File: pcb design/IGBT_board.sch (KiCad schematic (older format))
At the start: 44 parts, among them Q1 IGBT, Q10 IGBT, Q11 IGBT, Q12 IGBT, Q2 IGBT, Q3 IGBT, Q4 IGBT, Q5 IGBT, Q6 IGBT, Q7 IGBT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

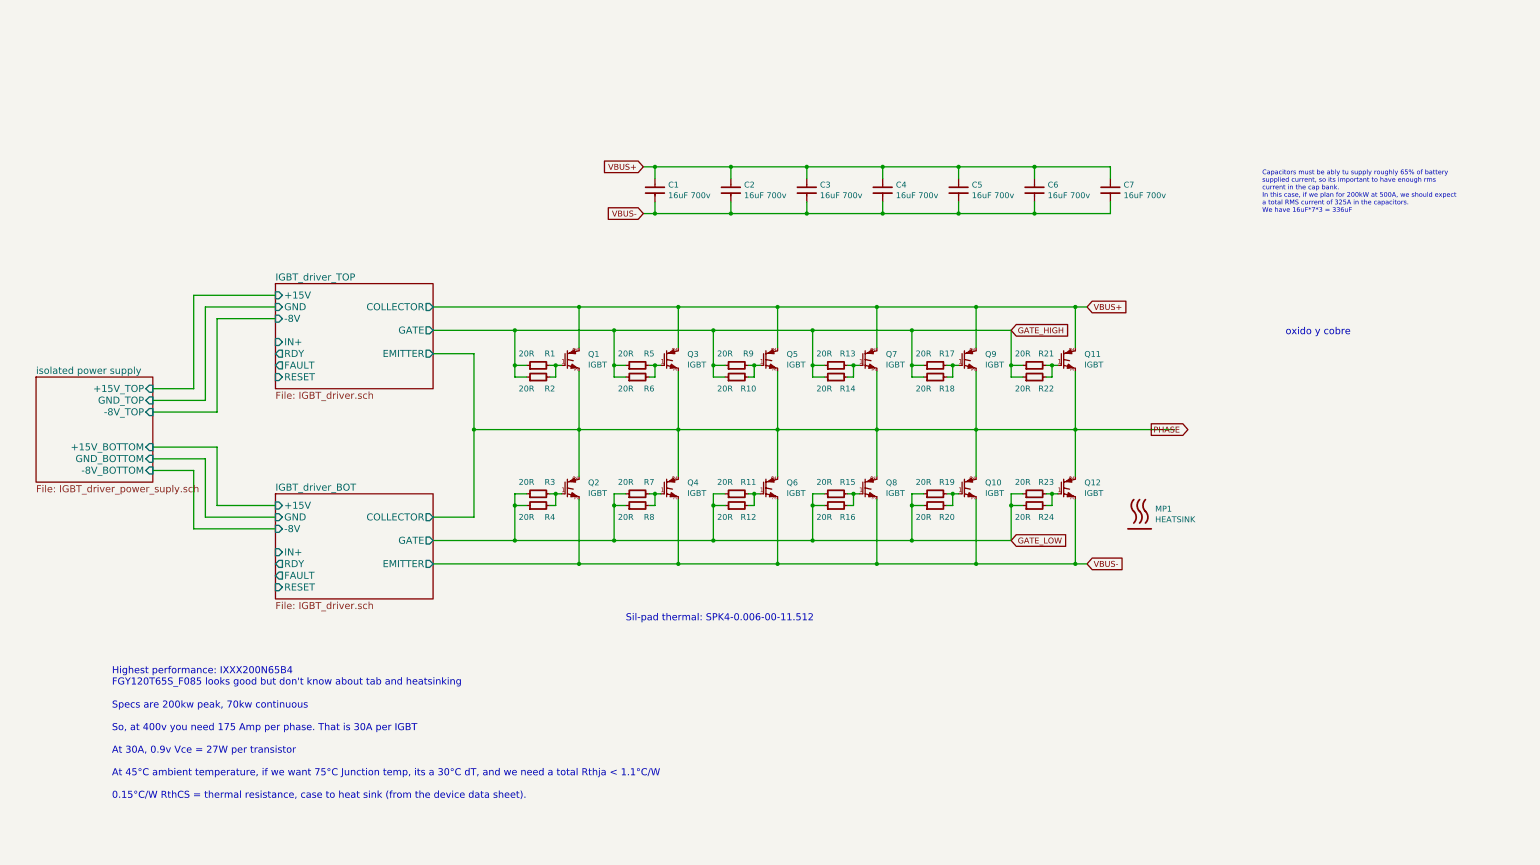
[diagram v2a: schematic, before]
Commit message: Add footprints, more layout and graphics
Signed-off-by: Marcos Chaparro <mchaparro@paltatech.com>
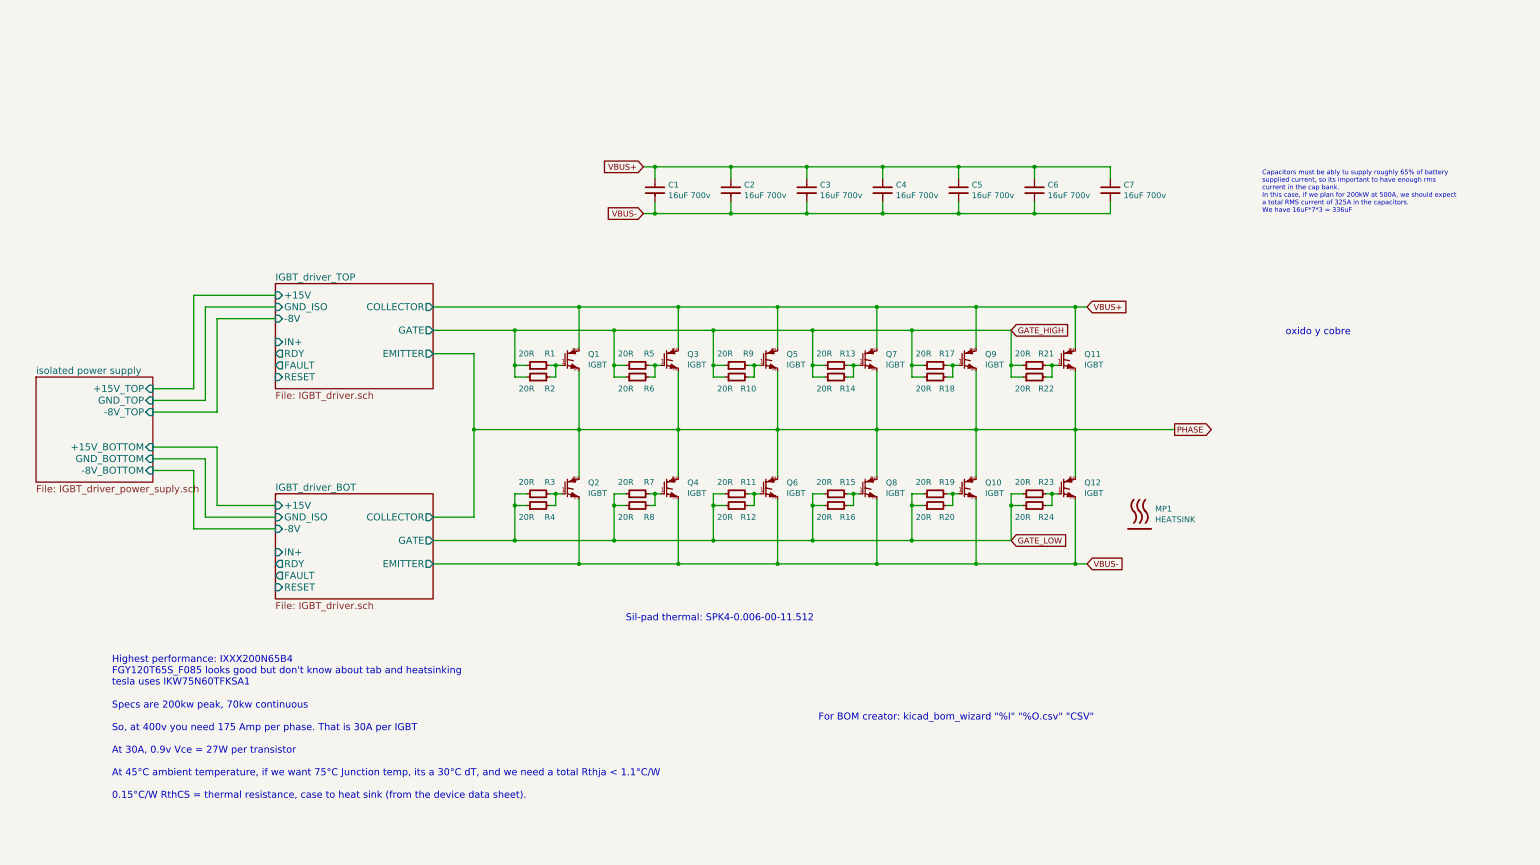
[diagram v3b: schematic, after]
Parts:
- Q10, Q11, Q12, Q2, Q3, Q4, Q5, Q6, Q7, Q8, Q9: mfg# IXXH80N65B4-ND -> IXXX110N65B4H1
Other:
- note added: "For BOM creator: kicad_bom_wizard "%I" "%O.csv" "CSV""
- note added: "Highest performance: IXXX200N65B4\nFGY120T65S_F085 looks good but don't know about tab and heatsinking\ntesla uses IKW75N60TFKSA1"
- note removed: "Highest performance: IXXX200N65B4\nFGY120T65S_F085 looks good but don't know about tab and heatsinking"
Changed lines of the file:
@@
 encoding utf-8
 Sheet 1 4
-Title ""
-Date ""
-Rev ""
-Comp ""
+Title "IGBT module"
+Date "2016-11-09"
+Rev "A"
+Comp "PALTA TECH"
 Comment1 ""
 Comment2 ""
@@
 F 2 "pth-semi:TO-247" H 6227 3409 60  0001 L CNN
 F 3 "" H 6100 3550 60  0000 C CNN
-F 4 "IXXH80N65B4-ND" H 6100 3500 60  0001 C CNN "mfg#"
+F 4 "IXXX110N65B4H1" H 6100 3500 60  0001 C CNN "mfg#"
 	1    6100 3500
 	1    0    0    -1
 $EndComp
 Text Notes 1300 6300 0    60   ~ 0
-Highest performance: IXXX200N65B4\nFGY120T65S_F085 looks good but don't know about tab and heatsinking
+Highest performance: IXXX200N65B4\nFGY120T65S_F085 looks good but don't know about tab and heatsinking\ntesla uses IKW75N60TFKSA1
 $Comp
 L R-2512 R1
@@
 F 2 "pth-semi:TO-247" H 5250 4650 60  0001 C CNN
 F 3 "" H 5250 4650 60  0000 C CNN
-F 4 "IXXH80N65B4-ND" H 5250 4600 60  0001 C CNN "mfg#"
+F 4 "IXXX110N65B4H1" H 5250 4600 60  0001 C CNN "mfg#"
 	1    5250 4600
 	1    0    0    -1
@@
 F 2 "pth-semi:TO-247" H 6100 4650 60  0001 C CNN
 F 3 "" H 6100 4650 60  0000 C CNN
-F 4 "IXXH80N65B4-ND" H 6100 4600 60  0001 C CNN "mfg#"
+F 4 "IXXX110N65B4H1" H 6100 4600 60  0001 C CNN "mfg#"
 	1    6100 4600
 	1    0    0    -1
@@
 F 2 "pth-semi:TO-247" H 7077 3409 60  0001 L CNN
 F 3 "" H 6950 3550 60  0000 C CNN
-F 4 "IXXH80N65B4-ND" H 6950 3500 60  0001 C CNN "mfg#"
+F 4 "IXXX110N65B4H1" H 6950 3500 60  0001 C CNN "mfg#"
 	1    6950 3500
 	1    0    0    -1
@@
 F 2 "pth-semi:TO-247" H 7800 3550 60  0001 C CNN
 F 3 "" H 7800 3550 60  0000 C CNN
-F 4 "IXXH80N65B4-ND" H 7800 3500 60  0001 C CNN "mfg#"
+F 4 "IXXX110N65B4H1" H 7800 3500 60  0001 C CNN "mfg#"
 	1    7800 3500
 	1    0    0    -1
@@
 F 2 "pth-semi:TO-247" H 6950 4650 60  0001 C CNN
 F 3 "" H 6950 4650 60  0000 C CNN
-F 4 "IXXH80N65B4-ND" H 6950 4600 60  0001 C CNN "mfg#"
+F 4 "IXXX110N65B4H1" H 6950 4600 60  0001 C CNN "mfg#"
 	1    6950 4600
 	1    0    0    -1
@@
 F 2 "pth-semi:TO-247" H 7800 4650 60  0001 C CNN
 F 3 "" H 7800 4650 60  0000 C CNN
-F 4 "IXXH80N65B4-ND" H 7800 4600 60  0001 C CNN "mfg#"
+F 4 "IXXX110N65B4H1" H 7800 4600 60  0001 C CNN "mfg#"
 	1    7800 4600
 	1    0    0    -1
@@
 F 2 "pth-semi:TO-247" H 8650 3550 60  0001 C CNN
 F 3 "" H 8650 3550 60  0000 C CNN
-F 4 "IXXH80N65B4-ND" H 8650 3500 60  0001 C CNN "mfg#"
+F 4 "IXXX110N65B4H1" H 8650 3500 60  0001 C CNN "mfg#"
 	1    8650 3500
 	1    0    0    -1
@@
 F 2 "pth-semi:TO-247" H 9500 3550 60  0001 C CNN
 F 3 "" H 9500 3550 60  0000 C CNN
-F 4 "IXXH80N65B4-ND" H 9500 3500 60  0001 C CNN "mfg#"
+F 4 "IXXX110N65B4H1" H 9500 3500 60  0001 C CNN "mfg#"
 	1    9500 3500
 	1    0    0    -1
@@
 F 2 "pth-semi:TO-247" H 8650 4650 60  0001 C CNN
 F 3 "" H 8650 4650 60  0000 C CNN
-F 4 "IXXH80N65B4-ND" H 8650 4600 60  0001 C CNN "mfg#"
+F 4 "IXXX110N65B4H1" H 8650 4600 60  0001 C CNN "mfg#"
 	1    8650 4600
 	1    0    0    -1
@@
 F 2 "pth-semi:TO-247" H 9500 4650 60  0001 C CNN
 F 3 "" H 9500 4650 60  0000 C CNN
-F 4 "IXXH80N65B4-ND" H 9500 4600 60  0001 C CNN "mfg#"
+F 4 "IXXX110N65B4H1" H 9500 4600 60  0001 C CNN "mfg#"
 	1    9500 4600
 	1    0    0    -1
@@
 GATE_LOW
 Connection ~ 4750 5050
-Text GLabel 10200 4100 2    50   Output ~ 0
+Text GLabel 10400 4100 2    50   Output ~ 0
 PHASE
 $Comp
@@
 F0 "IGBT_driver_TOP" 60
 F1 "IGBT_driver.sch" 60
-F2 "GND" I L 2700 3050 60
-F3 "+15V" I L 2700 2950 60
-F4 "-8V" I L 2700 3150 60
-F5 "IN+" I L 2700 3350 60
-F6 "GATE" O R 4050 3250 60
-F7 "COLLECTOR" O R 4050 3050 60
-F8 "EMITTER" O R 4050 3450 60
-F9 "RDY" O L 2700 3450 60
-F10 "FAULT" O L 2700 3550 60
-F11 "RESET" I L 2700 3650 60
+F2 "+15V" I L 2700 2950 60
+F3 "-8V" I L 2700 3150 60
+F4 "IN+" I L 2700 3350 60
+F5 "GATE" O R 4050 3250 60
+F6 "COLLECTOR" O R 4050 3050 60
+F7 "EMITTER" O R 4050 3450 60
+F8 "RDY" O L 2700 3450 60
+F9 "FAULT" O L 2700 3550 60
+F10 "RESET" I L 2700 3650 60
+F11 "GND_ISO" I L 2700 3050 60
 $EndSheet
 $Sheet
@@
 F0 "IGBT_driver_BOT" 60
 F1 "IGBT_driver.sch" 60
-F2 "GND" I L 2700 4850 60
-F3 "+15V" I L 2700 4750 60
-F4 "-8V" I L 2700 4950 60
-F5 "IN+" I L 2700 5150 60
-F6 "GATE" O R 4050 5050 60
-F7 "COLLECTOR" O R 4050 4850 60
-F8 "EMITTER" O R 4050 5250 60
-F9 "RDY" O L 2700 5250 60
-F10 "FAULT" O L 2700 5350 60
-F11 "RESET" I L 2700 5450 60
+F2 "+15V" I L 2700 4750 60
+F3 "-8V" I L 2700 4950 60
+F4 "IN+" I L 2700 5150 60
+F5 "GATE" O R 4050 5050 60
+F6 "COLLECTOR" O R 4050 4850 60
+F7 "EMITTER" O R 4050 5250 60
+F8 "RDY" O L 2700 5250 60
+F9 "FAULT" O L 2700 5350 60
+F10 "RESET" I L 2700 5450 60
+F11 "GND_ISO" I L 2700 4850 60
 $EndSheet
 Wire Wire Line
@@
 Wire Wire Line
 	2000 4450 1650 4450
+Text Notes 7350 6600 0    60   ~ 0
+For BOM creator: kicad_bom_wizard "%I" "%O.csv" "CSV"
 $EndSCHEMATC

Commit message: Larger gate resistors, added gate caps, added comments and images to the schematic
Signed-off-by: Marcos Chaparro <mchaparro@paltatech.com>
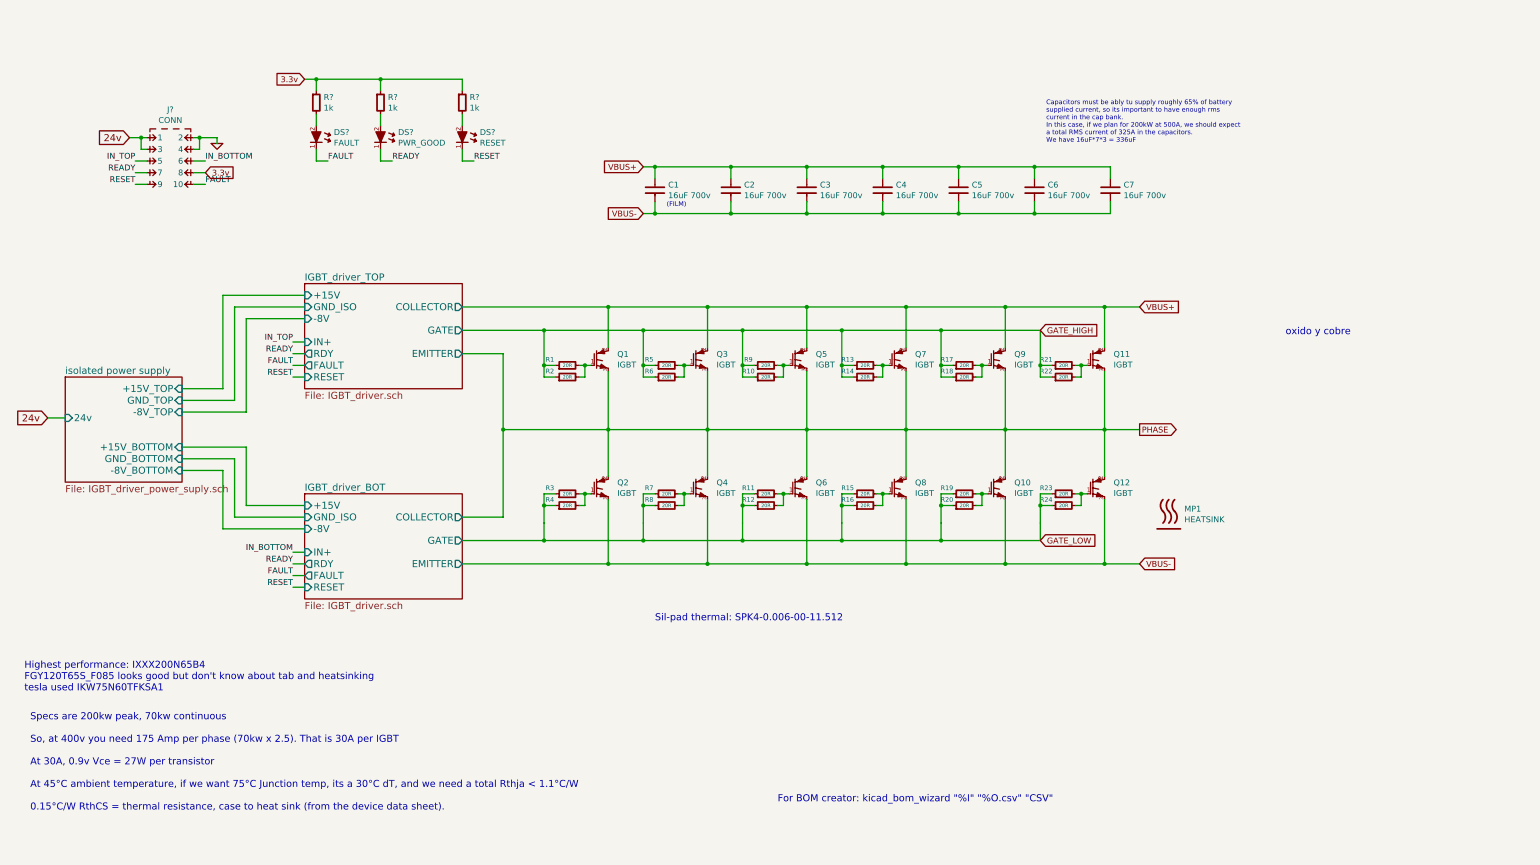
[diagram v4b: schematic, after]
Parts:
- added DS?: FAULT, smd-semi:LED-0603, symbol LED-0603
- added DS?: PWR_GOOD, smd-semi:LED-0603, symbol LED-0603
- added DS?: RESET, smd-semi:LED-0603, symbol LED-0603
- added J?: CONN, conn-100mil:CONN-100MIL-M-2x5, symbol CONN-100MIL-M-2x5
- added R? (x3): 1k, IPC7351-Nominal:RESC1608X50, symbol R-0603
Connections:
- new net: DS?.2 (A), R?.2 (x3)
- new net 24v: J?.1, J?.3
- new net 3.3v: J?.8, R?.1, R?.1, R?.1
- new net FAULT: DS?.1 (K), J?.10
- new net GND: J?.2, J?.4
- new net IN_BOTTOM: J?.6
- new net IN_TOP: J?.5
- new net READY: DS?.1 (K), J?.7
- new net RESET: DS?.1 (K), J?.9
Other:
- note added: "(FILM)"
- note added: "Highest performance: IXXX200N65B4\nFGY120T65S_F085 looks good but don't know about tab and heatsinking\ntesla used IKW75N60TFKSA1"
- note added: "Specs are 200kw peak, 70kw continuous\n\nSo, at 400v you need 175 Amp per phase (70kw x 2.5). That is 30A per IGBT\n\nAt 30A, 0.9v Vce = 27W per transistor\n\nAt 45°C ambient temperature, if we want 75°C Junction temp, its a 30°C dT, and we need a total Rthja < 1.1°C/W\n\n0.15°C/W RthCS = thermal resistance, case to heat sink (from the device data sheet). \n\n\n\n\n\n\n"
- note removed: "Highest performance: IXXX200N65B4\nFGY120T65S_F085 looks good but don't know about tab and heatsinking\ntesla uses IKW75N60TFKSA1"
- note removed: "Specs are 200kw peak, 70kw continuous\n\nSo, at 400v you need 175 Amp per phase. That is 30A per IGBT\n\nAt 30A, 0.9v Vce = 27W per transistor\n\nAt 45°C ambient temperature, if we want 75°C Junction temp, its a 30°C dT, and we need a total Rthja < 1.1°C/W\n\n0.15°C/W RthCS = thermal resistance, case to heat sink (from the device data sheet). \n\n\n\n\n\n\n"
- moved on the sheet: MP1, Q1, Q10, Q11, Q12, Q2, Q3, Q4, Q5, Q6, Q7, Q8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

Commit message: Added 3D models, connector, more layout, updated readme
Signed-off-by: Marcos Chaparro <mchaparro@paltatech.com>
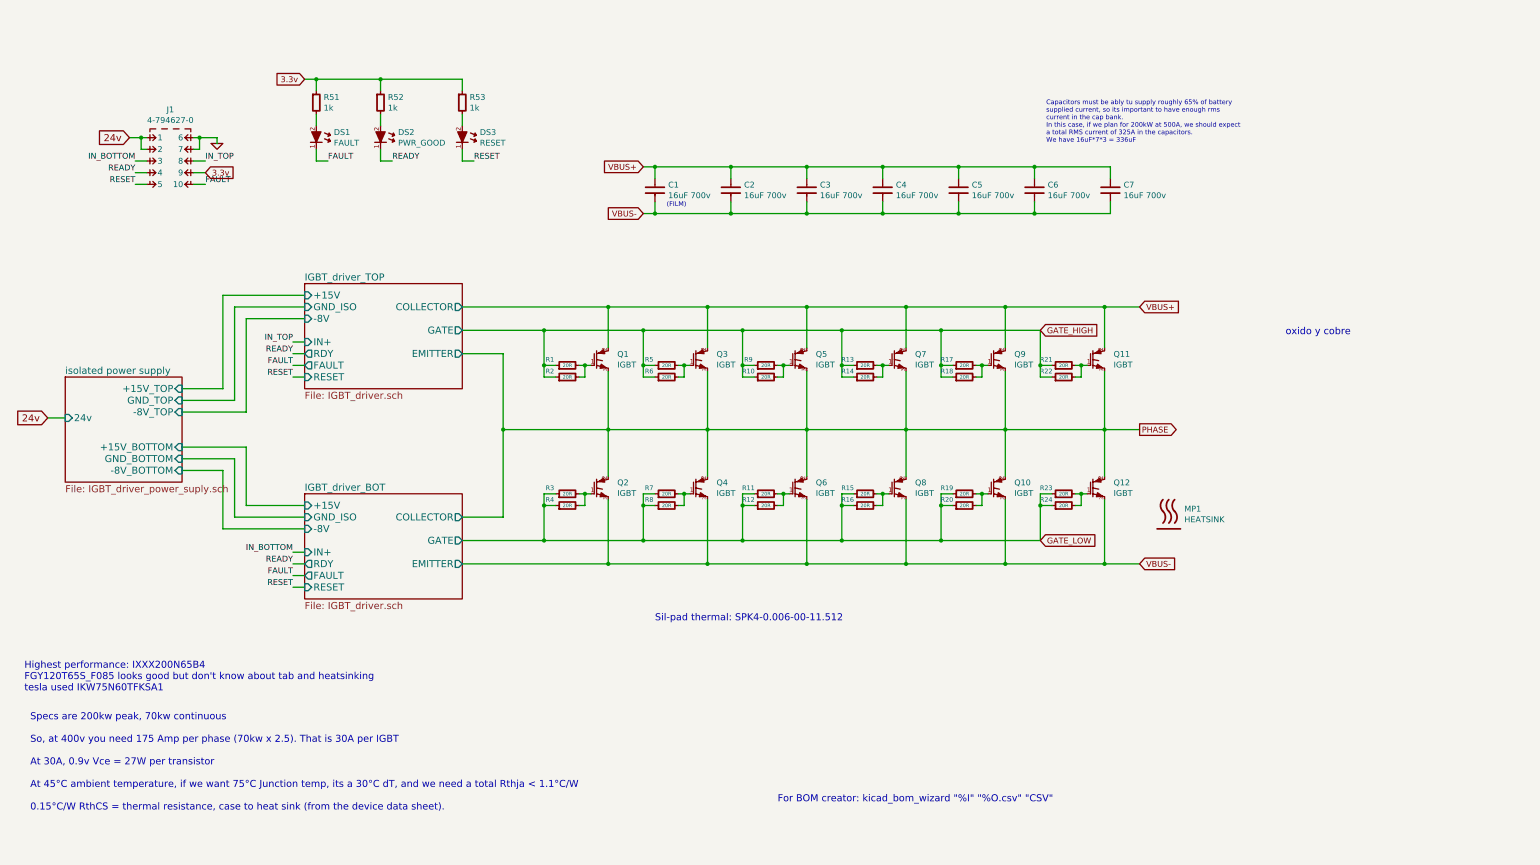
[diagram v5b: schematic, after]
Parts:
- removed J?: CONN, conn-100mil:CONN-100MIL-M-2x5, symbol CONN-100MIL-M-2x5
- added J1: 4-794627-0, paltatech:TE-4-794627-0, symbol 4-794627-0
- gave numbers to parts that had none: 6
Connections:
- net 24v: now also J1.1, J1.2
- net 3.3v: now also J1.9
- net FAULT: now also J1.10
- net GND: now also J1.6, J1.7
- net IN_BOTTOM: now also J1.3
- net IN_TOP: now also J1.8
- net READY: now also J1.4
- net RESET: now also J1.5

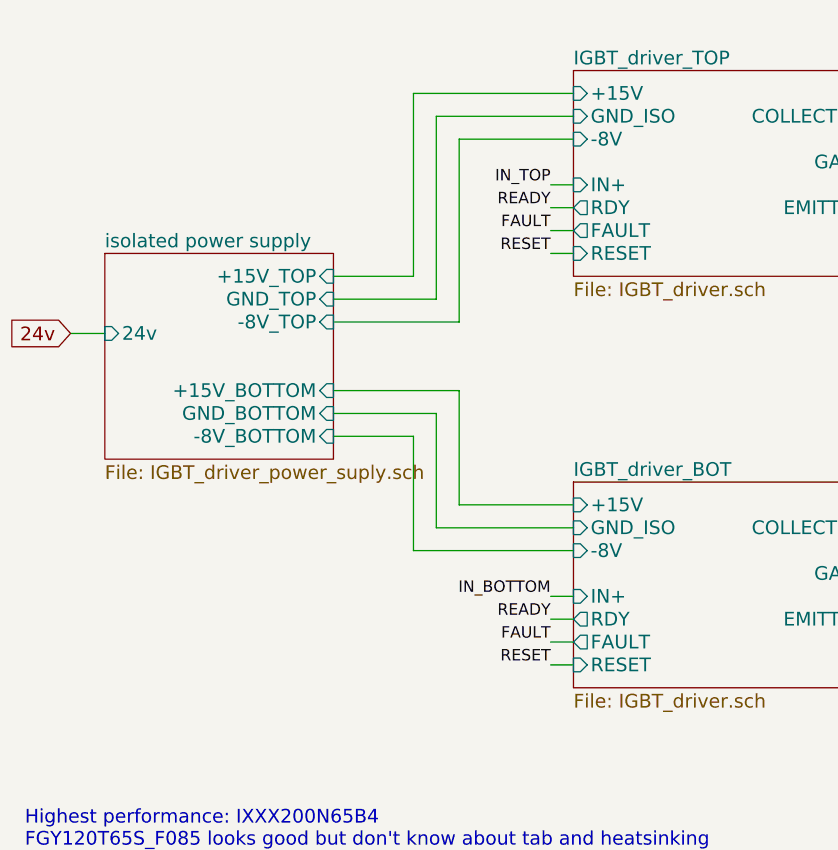
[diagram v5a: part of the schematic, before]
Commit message: Added testpoints
Signed-off-by: Marcos Chaparro <mchaparro@paltatech.com>
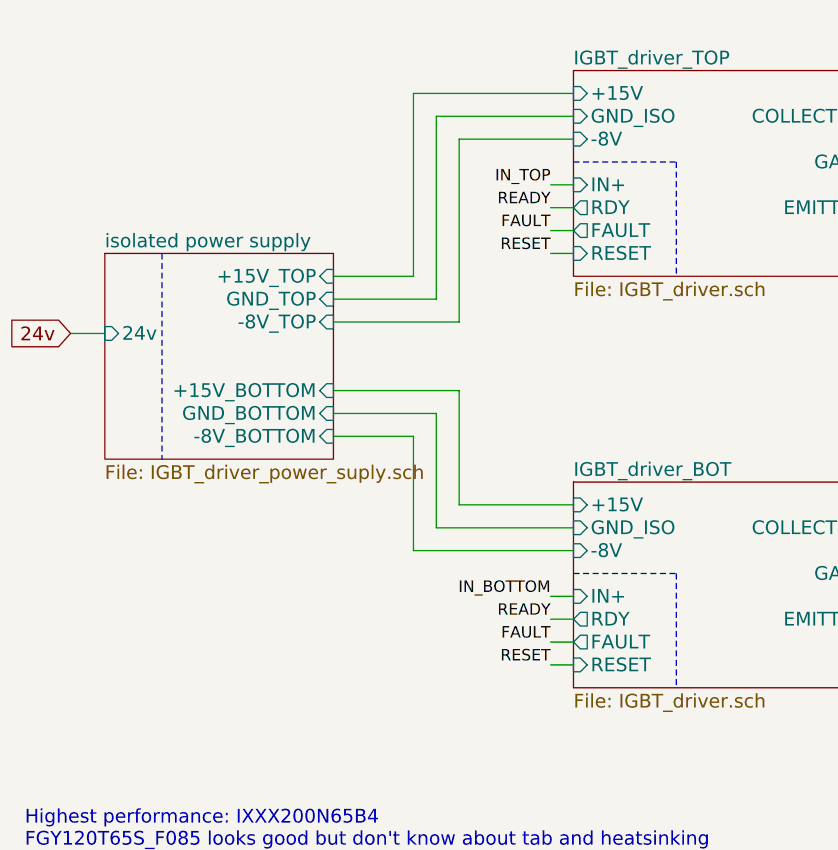
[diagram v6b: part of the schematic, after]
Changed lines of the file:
@@
 Connection ~ 1550 1600
 $Comp
-L GND #PWR01
+L GND #PWR1
 U 1 1 5831A3A1
 P 2200 1650
-F 0 "#PWR01" H 2200 1650 30  0001 C CNN
+F 0 "#PWR1" H 2200 1650 30  0001 C CNN
 F 1 "GND" H 2200 1580 30  0001 C CNN
 F 2 "" H 2200 1650 60  0000 C CNN
@@
 	1    0    0    -1
 $EndComp
+Wire Notes Line
+	2950 3250 3400 3250
+Wire Notes Line
+	3400 3250 3400 3750
+Wire Notes Line
+	2950 5050 3400 5050
+Wire Notes Line
+	3400 5050 3400 5550
+Wire Notes Line
+	1150 3650 1150 4550
 $EndSCHEMATC
